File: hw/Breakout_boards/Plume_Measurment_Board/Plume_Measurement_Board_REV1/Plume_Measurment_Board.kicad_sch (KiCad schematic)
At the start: 15 parts, among them J1 Conn_Coaxial, U1 AD7124-8BCPZ-RL

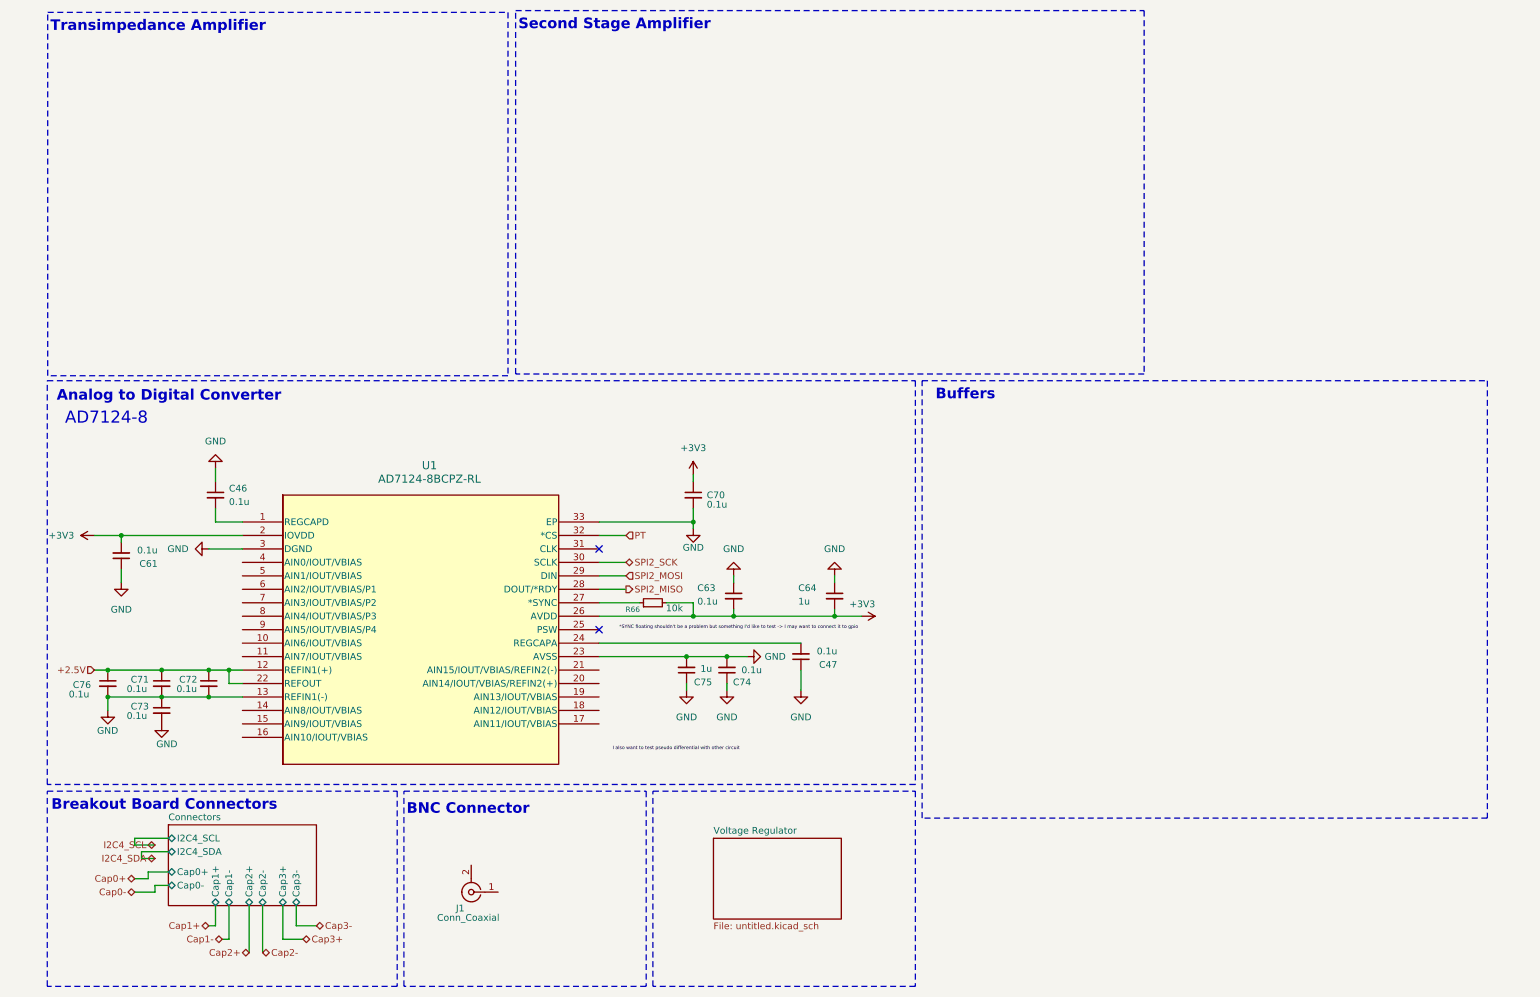
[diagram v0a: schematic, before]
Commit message: Addedd Symbols Libraries
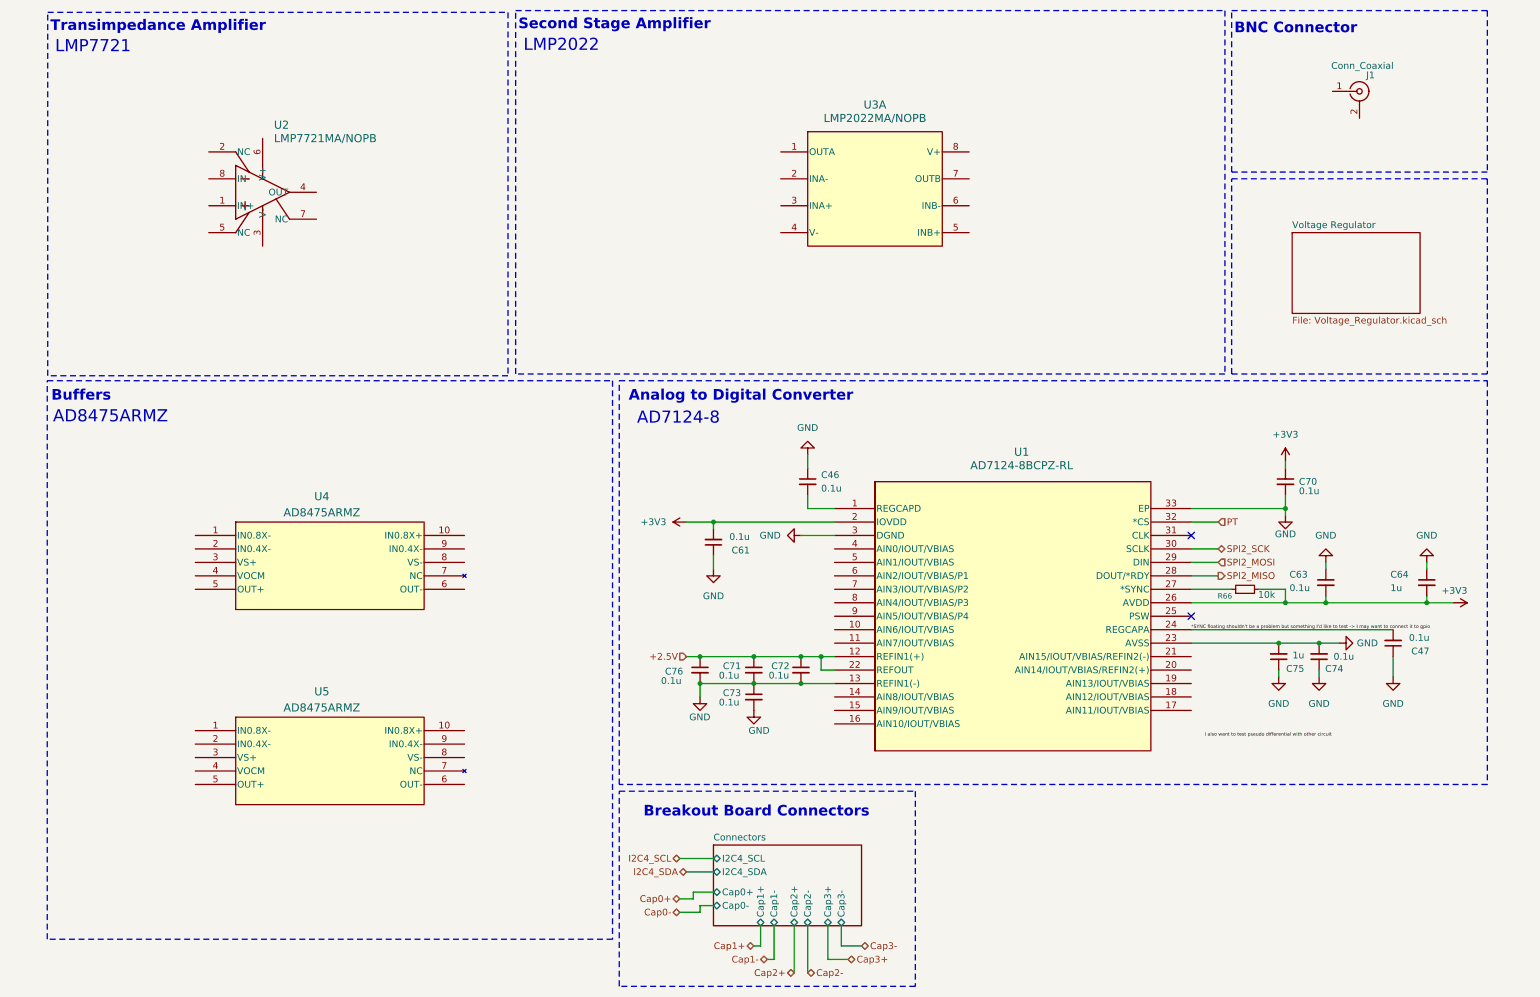
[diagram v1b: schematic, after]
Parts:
- added U2: LMP7721MA/NOPB, M08A, symbol Amplifier_Texas_Instruments:LMP7721MA_NOPB
- added U3: LMP2022MA/NOPB, M08A, symbol Amplifier_Texas_Instruments:LMP2022MA_NOPB
- added U4, U5: AD8475ARMZ, RM_10_ADI, symbol Amplifier_Buffer_Texas_Instruments:AD8475ARMZ
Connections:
- net *SYNC floating shouldn't be a problem but something I'd like to test -> I may want to connect it to gpio: now also C47.2, U1.24 (REGCAPA)
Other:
- sheet Voltage Regulator: file untitled.kicad_sch -> Voltage_Regulator.kicad_sch
- note added: "AD8475ARMZ"
- note added: "LMP2022"
- note added: "LMP7721"
- moved on the sheet: C46, C47, C61, C63, C64, C70, C71, C72, C73, C74, C75, C76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

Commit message: Orgnanization Between Pages
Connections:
- net PT renamed PM_CS
- net SPI2_MISO renamed SPI1_MISO
- net SPI2_MOSI renamed SPI1_MOSI
- net SPI2_SCK renamed SPI1_SCK
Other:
- sheet Connectors ports: added +VBAT, 3V3, PM_CS, Plume, SPI1_CLK, SPI1_MISO, SPI1_MOSI; removed Cap0+, Cap0-, Cap1+, Cap1-, Cap2+, Cap2-, Cap3+, Cap3-, I2C4_SCL, I2C4_SDA
- sheet Voltage Regulator ports: added +VBAT; removed none
- moved on the sheet: J1, U3A

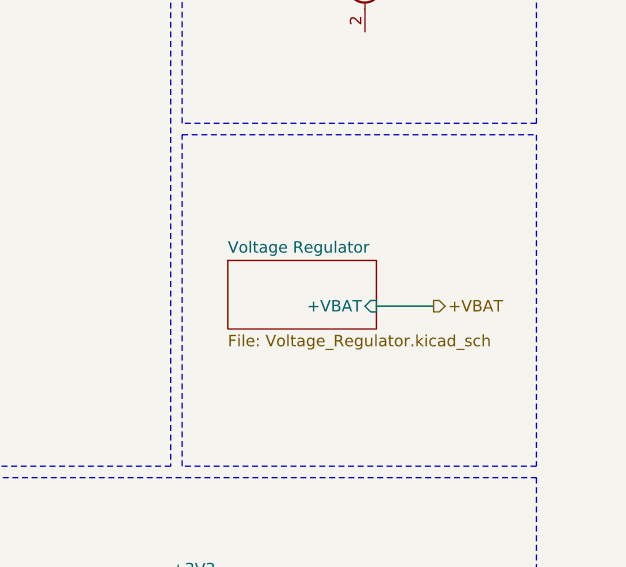
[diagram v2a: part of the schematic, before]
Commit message: 5V Voltage Regulator Addition
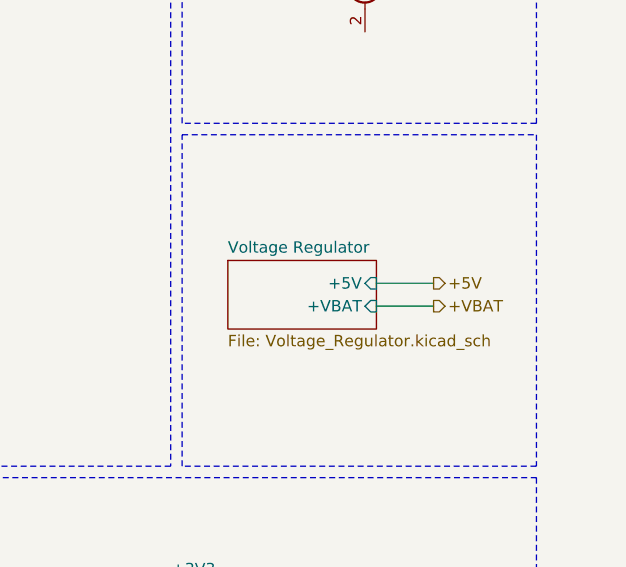
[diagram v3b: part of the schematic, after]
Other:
- sheet Voltage Regulator ports: added +5V; removed none
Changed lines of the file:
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@@
 	(wire
 		(pts
-			(xy 266.7 63.5) (xy 273.05 63.5)
+			(xy 246.38 104.14) (xy 246.38 106.68)
 		)
 		(stroke
@@
 	(wire
 		(pts
-			(xy 246.38 104.14) (xy 246.38 106.68)
+			(xy 133.35 179.07) (xy 135.89 179.07)
 		)
 		(stroke
@@
 	(wire
 		(pts
-			(xy 133.35 179.07) (xy 135.89 179.07)
+			(xy 245.11 132.08) (xy 252.73 132.08)
 		)
 		(stroke
@@
 	(wire
 		(pts
-			(xy 245.11 132.08) (xy 252.73 132.08)
+			(xy 156.21 96.52) (xy 156.21 99.06)
 		)
 		(stroke
@@
 	(wire
 		(pts
-			(xy 156.21 96.52) (xy 156.21 99.06)
+			(xy 135.89 139.7) (xy 146.05 139.7)
 		)
 		(stroke
@@
 	(wire
 		(pts
-			(xy 135.89 139.7) (xy 146.05 139.7)
+			(xy 158.75 137.16) (xy 158.75 134.62)
 		)
 		(stroke
@@
 	(wire
 		(pts
-			(xy 158.75 137.16) (xy 158.75 134.62)
+			(xy 156.21 104.14) (xy 156.21 106.68)
 		)
 		(stroke
@@
 	(wire
 		(pts
-			(xy 156.21 104.14) (xy 156.21 106.68)
+			(xy 266.7 60.96) (xy 273.05 60.96)
 		)
 		(stroke
@@
 	(wire
 		(pts
+			(xy 266.7 63.5) (xy 273.05 63.5)
+		)
+		(stroke
+			(width 0)
+			(type default)
+		)
+	)
+	(wire
+		(pts
 			(xy 273.05 124.46) (xy 278.13 124.46)
 		)
@@
 		)
 	)
+	(hierarchical_label "+5V"
+		(shape output)
+		(at 273.05 60.96 0)
+		(effects
+			(font
+				(size 1.27 1.27)
+			)
+			(justify left)
+		)
+	)
 	(hierarchical_label "SPI1_SCK"
 		(shape bidirectional)
@@
 			(effects
 				(font
+					(size 1.27 1.27)
+				)
+				(justify right)
+			)
+		)
+		(pin "+5V" input
+			(at 266.7 60.96 0)
+			(effects
+				(font

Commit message: Connector Fixes
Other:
- note added: "V_out = - I * R_G"
- company: (none) -> Electric Propulsion Lab
- title: (none) -> Plume Measurement Board
- moved on the sheet: U3A

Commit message: Amplifier
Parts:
- removed J1: Conn_Coaxial, symbol Connector:Conn_Coaxial
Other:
- note added: "5V Regulator"
- note added: "Pico-Ammeter Design Inspiration: https://repository.lsu.edu/honors_etd/1432/"
- note added: "V_out = - (R_feedback / Rf_in) * V_in"
- note added: "V_out = - I_in * R_feedback + V_offs"
- note removed: "BNC Connector"
- note removed: "V_out = - I * R_G"
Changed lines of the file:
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@@
 	)
 	(rectangle
-		(start 245.11 44.45)
+		(start 245.11 12.7)
 		(end 284.48 81.28)
 		(stroke
@@
 		)
 	)
-	(rectangle
-		(start 245.11 12.7)
-		(end 284.48 43.18)
-		(stroke
-			(width 0)
-			(type dash)
-		)
-		(fill
-			(type none)
+	(text "V_out = - (R_feedback /  Rf_in) * V_in"
+		(exclude_from_sim no)
+		(at 138.938 78.74 0)
+		(effects
+			(font
+				(size 2.286 2.286)
+				(italic yes)
+			)
 		)
 	)
@@
 		)
 	)
-	(text "V_out = - I * R_G\n\n"
+	(text "V_out = - I_in * R_feedback + V_offs\n\n\n"
 		(exclude_from_sim no)
-		(at 30.988 80.01 0)
+		(at 47.752 83.312 0)
 		(effects
 			(font
@@
 		)
 	)
-	(text "BNC Connector"
+	(text "5V Regulator"
 		(exclude_from_sim no)
-		(at 245.618 17.018 0)
+		(at 246.126 16.764 0)
 		(effects
 			(font
@@
 		)
 	)
+	(text "Pico-Ammeter Design Inspiration: https://repository.lsu.edu/honors_etd/1432/"
+		(exclude_from_sim no)
+		(at 52.832 194.818 0)
+		(effects
+			(font
+				(size 1.27 1.27)
+			)
+		)
+	)
 	(junction
 		(at 245.11 132.08)
@@
 	(wire
 		(pts
-			(xy 266.7 60.96) (xy 275.59 60.96)
+			(xy 266.7 44.45) (xy 275.59 44.45)
 		)
 		(stroke
@@
 	(wire
 		(pts
-			(xy 266.7 63.5) (xy 273.05 63.5)
+			(xy 266.7 46.99) (xy 273.05 46.99)
 		)
 		(stroke
@@
 	(wire
 		(pts
-			(xy 275.59 55.88) (xy 275.59 60.96)
+			(xy 275.59 39.37) (xy 275.59 44.45)
 		)
 		(stroke
@@
 	)
 	(hierarchical_label "+VBAT"
-		(shape output)
-		(at 273.05 63.5 0)
+		(shape input)
+		(at 273.05 46.99 0)
 		(effects
 			(font
@@
 	)
 	(hierarchical_label "+VBAT"
-		(shape output)
+		(shape input)
 		(at 165.1 182.88 0)
 		(effects
@@
 	(symbol
 		(lib_id "power:+3V3")
-		(at 275.59 55.88 0)
+		(at 275.59 39.37 0)
 		(unit 1)
 		(body_style 1)
@@
 		(fields_autoplaced yes)
 		(property "Reference" "#PWR0244"
-			(at 275.59 59.69 0)
+			(at 275.59 43.18 0)
 			(hide yes)
 			(show_name no)
@@
 		)
 		(property "Value" "+5V"
-			(at 275.59 50.8 0)
+			(at 275.59 34.29 0)
 			(show_name no)
 			(do_not_autoplace no)
@@
 		)
 		(property "Footprint" ""
-			(at 275.59 55.88 0)
+			(at 275.59 39.37 0)
 			(hide yes)
 			(show_name no)
@@
 		)
 		(property "Datasheet" ""
-			(at 275.59 55.88 0)
+			(at 275.59 39.37 0)
 			(hide yes)
 			(show_name no)
@@
 		)
 		(property "Description" "Power symbol creates a global label with name \"+3V3\""
-			(at 275.59 55.88 0)
+			(at 275.59 39.37 0)
 			(hide yes)
 			(show_name no)
@@
 	)
 	(symbol
-		(lib_id "Connector:Conn_Coaxial")
-		(at 265.43 27.94 0)
-		(unit 1)
-		(body_style 1)
-		(exclude_from_sim no)
-		(in_bom yes)
-		(on_board yes)
-		(in_pos_files yes)
-		(dnp no)
-		(property "Reference" "J1"
-			(at 266.7 24.892 0)
-			(show_name no)
-			(do_not_autoplace no)
-			(effects
-				(font
-					(size 1.27 1.27)
-				)
-				(justify left)
-			)
-		)
-		(property "Value" "Conn_Coaxial"
-			(at 260.096 23.114 0)
-			(show_name no)
-			(do_not_autoplace no)
-			(effects
-				(font
-					(size 1.27 1.27)
-				)
-				(justify left)
-			)
-		)
-		(property "Footprint" ""
-			(at 265.43 27.94 0)
-			(hide yes)
-			(show_name no)
-			(do_not_autoplace no)
-			(effects
-				(font
-					(size 1.27 1.27)
-				)
-			)
-		)
-		(property "Datasheet" ""
-			(at 265.43 27.94 0)
-			(hide yes)
-			(show_name no)
-			(do_not_autoplace no)
-			(effects
-				(font
-					(size 1.27 1.27)
-				)
-			)
-		)
-		(property "Description" "coaxial connector (BNC, SMA, SMB, SMC, Cinch/RCA, LEMO, ...)"
-			(at 265.43 27.94 0)
-			(hide yes)
-			(show_name no)
-			(do_not_autoplace no)
-			(effects
-				(font
-					(size 1.27 1.27)
-				)
-			)
-		)
-		(pin "1"
-		)
-		(pin "2"
-		)
-		(instances
-			(project "Plume_Measurment_Board"
-				(path "/2e1d3673-27b9-4604-80fb-036cec98a912"
-					(reference "J1")
-					(unit 1)
-				)
-			)
-		)
-	)
-	(symbol
 		(lib_id "Device:C_Small")
 		(at 138.43 113.03 180)
@@
 	)
 	(sheet
-		(at 250.19 58.42)
+		(at 250.19 41.91)
 		(size 16.51 7.62)
 		(exclude_from_sim no)
@@
 		)
 		(property "Sheetname" "Voltage Regulator"
-			(at 250.19 57.7084 0)
+			(at 250.19 41.1984 0)
 			(show_name no)
 			(do_not_autoplace no)
@@
 		)
 		(property "Sheetfile" "Voltage_Regulator.kicad_sch"
-			(at 250.19 66.6246 0)
+			(at 250.19 50.1146 0)
 			(show_name no)
 			(do_not_autoplace no)
@@
 		)
 		(pin "+VBAT" input
-			(at 266.7 63.5 0)
+			(at 266.7 46.99 0)
 			(effects
 				(font
@@
 		)
 		(pin "+5V" input
-			(at 266.7 60.96 0)
+			(at 266.7 44.45 0)
 			(effects
 				(font
